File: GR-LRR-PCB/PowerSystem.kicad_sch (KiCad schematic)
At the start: 21 parts, among them IC1 TLV75533PDBVR, J1 +BATT, J2 -BATT

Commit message: starting first layout
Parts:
- added 24V1, 3.3V1, 5V1, GND1: TestPoint, TestPoint:TestPoint_Pad_D2.5mm, symbol Connector:TestPoint
- added J14: BATT VIN JUMPER, Connector_PinHeader_2.54mm:PinHeader_1x02_P2.54mm_Vertical, symbol Connector:Conn_01x02_Pin
- added J17: GND JUMPER, Connector_PinHeader_2.54mm:PinHeader_1x02_P2.54mm_Vertical, symbol Connector:Conn_01x02_Pin
- renumbered J1 to J3, J2 to J4
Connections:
- net +24V: now also 24V1.1
- net +3.3V: now also 3.3V1.1
- net +5V: now also 5V1.1
- net BATT_GND: now also J17.2 (Pin_2)
- net BATT_VIN: now also J14.1 (Pin_1)
- net GND: now also GND1.1, J17.1 (Pin_1)
- net at J3.1_1, J3.1_2, J3.2_1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: now also J14.2 (Pin_2)
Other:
- moved on the sheet: C0, C1, C2, C3, CY1, CY2, L1, PS2

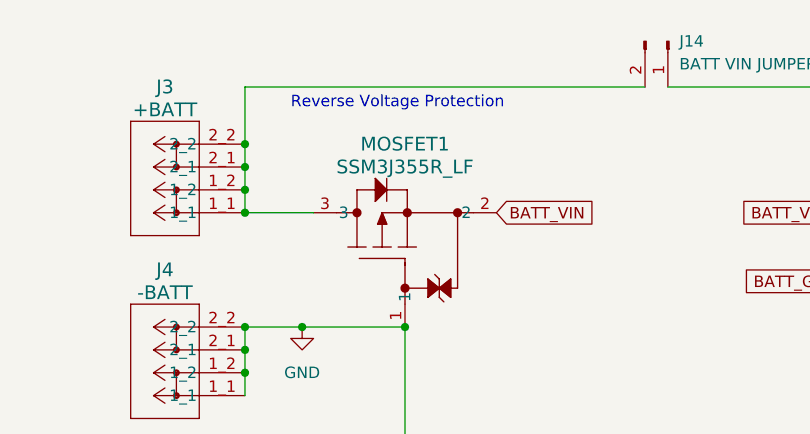
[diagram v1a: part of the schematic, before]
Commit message: new smaller layout
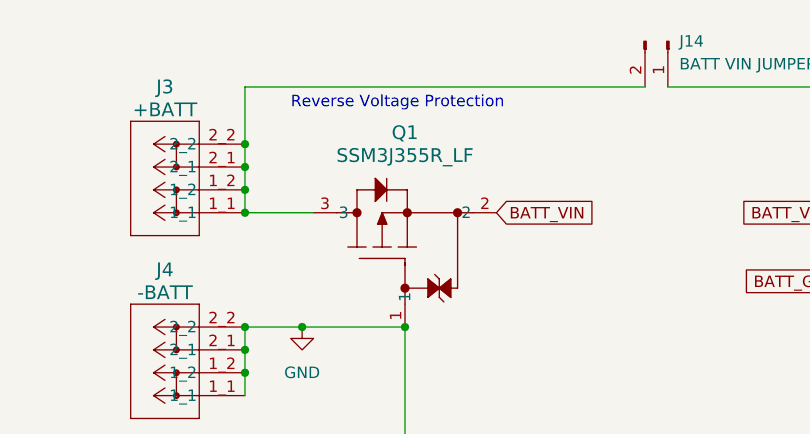
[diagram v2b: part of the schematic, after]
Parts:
- renumbered MOSFET1 to Q1
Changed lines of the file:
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@@
   (symbol (lib_id "SSM3J355R_LF:SSM3J355R_LF") (at 90.17 45.72 90) (unit 1)
     (in_bom yes) (on_board yes) (dnp no) (fields_autoplaced)
-    (property "Reference" "MOSFET1" (at 97.79 27.94 90)
+    (property "Reference" "Q1" (at 97.79 26.67 90)
       (effects (font (size 1.524 1.524)))
     )
-    (property "Value" "SSM3J355R_LF" (at 97.79 30.48 90)
+    (property "Value" "SSM3J355R_LF" (at 97.79 29.21 90)
       (effects (font (size 1.524 1.524)))
     )
@@
       (project "GR-LRR-PCB"
         (path "/f2632f9f-3f36-4af8-bf53-b0ff2066ae87/db65c721-ccfc-4bc9-b167-41780dab10e5"
-          (reference "MOSFET1") (unit 1)
+          (reference "Q1") (unit 1)
         )
       )
